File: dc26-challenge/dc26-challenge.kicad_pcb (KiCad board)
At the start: 2 copper layers, 107 x 107 mm, 0 parts

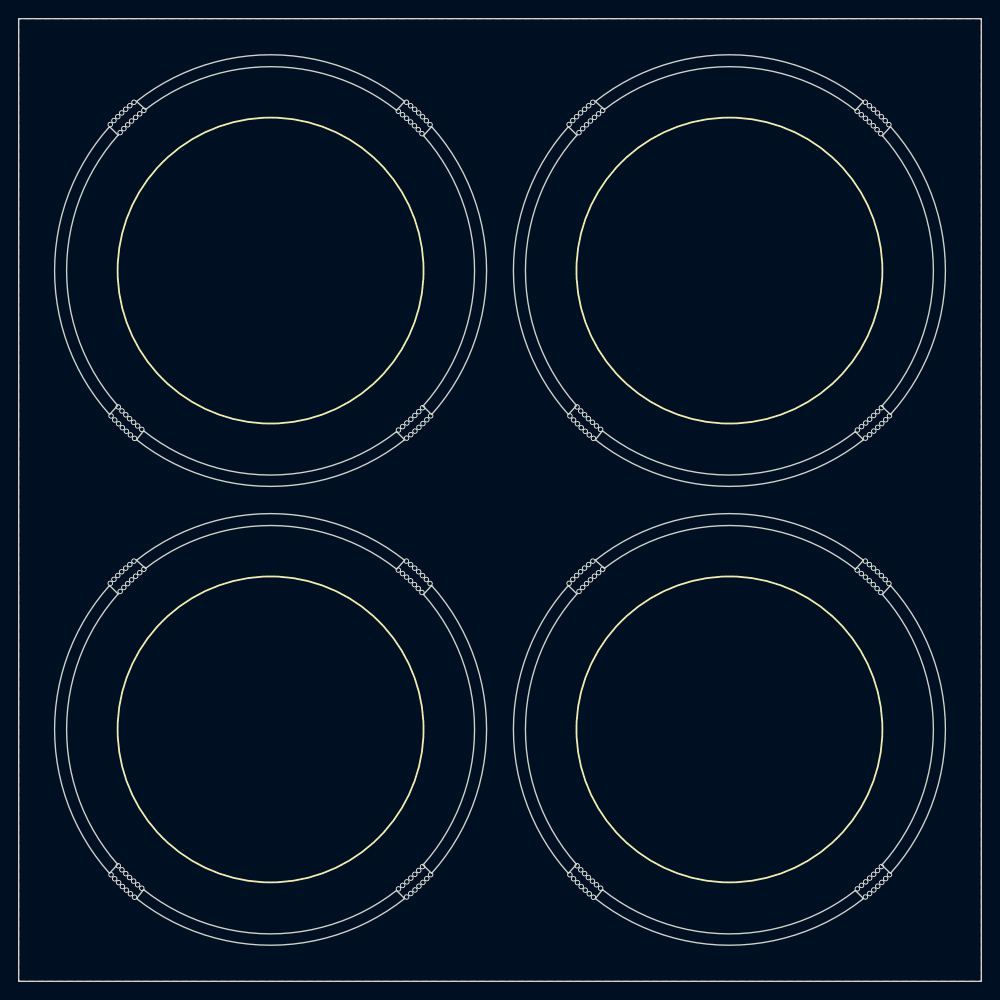
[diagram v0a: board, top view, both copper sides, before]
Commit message: Icons for challenge coins
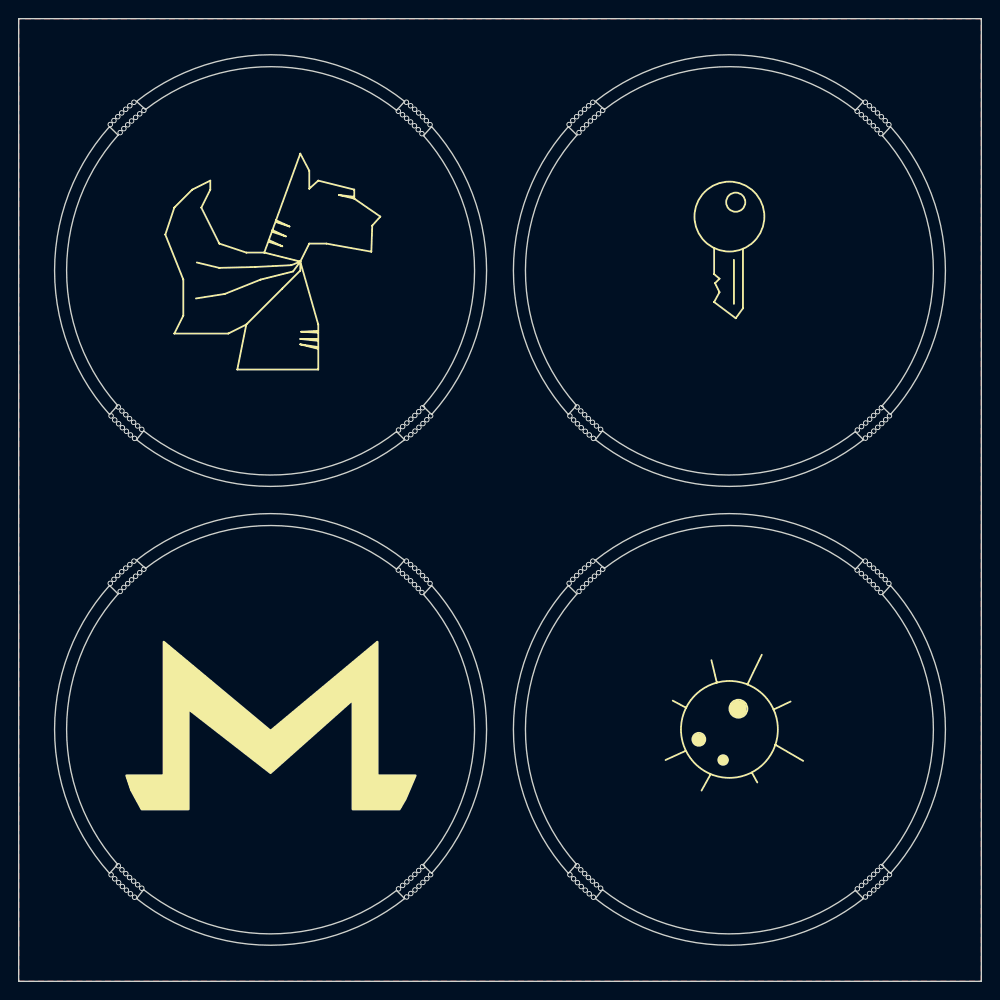
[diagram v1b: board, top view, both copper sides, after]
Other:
- board text added: "^"
